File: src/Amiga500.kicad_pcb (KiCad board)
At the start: 2 copper layers, 365.8 x 254 mm, 367 parts, among them CN1 LEFT_JOY, CN10 COMPOSITE, CN11 INTERNAL_FLOPPY, CN12 FLOPPY_POWER, CN13 KEYBOARD, CN14 IDE_POWER, CN15 IDE_I/F, CN2 RIGHT_JOY, CN3 RIGHT, CN4 LEFT, CN5 EXTFLOPPY_DB23F, CN6 SERIAL_DB25M, CN7 PARALLEL_DB25F, CN8 POWER, CN9 VIDEO_DB23M, J90 DRIVE_SWITCHER, J91 Dispatcher_3to1, J92 Dispatcher_3to1, J93 Dispatcher_3to1, J99 CONN_HDACT, P1 EXPANSION BUS, P9 TRAPDOOR, Q301 2N3906, Q321 MPF102, Q331 MPF102, Q501 2N3904, Q502 2N3906, Q503 2N3906, Q711 2N3904, Q921 MMBFJ113, Q931 MMBFJ113, Q99 2N3906, U1 68000D, U10 74LS244, U11 74LS373, U12 74LS244, U13 74LS373, U14 LF347, U15 74LS157, U16 XX4256, U17 XX4256, U18 XX4256, U19 XX4256, U2 FAT_AGNUS_8375, U20 XX4256, U21 XX4256, U22 XX4256, U23 XX4256, U3 PAULA, U32 74LS139, U33 74LS258, U34 74LS373, U35 74LS244, U36 74LS05, U37 74LS32, U38 MC1488, U39 MC1489, U4 DENISE, U40 74LS245, U41 74LS245, U42 NE555, U5 GARY_5719, U6 ROM, U7 VIA_8520, U8 VIA_8520, U9 MSM6242B, U94 74HCT14, X1 XTAL, Y9 32768

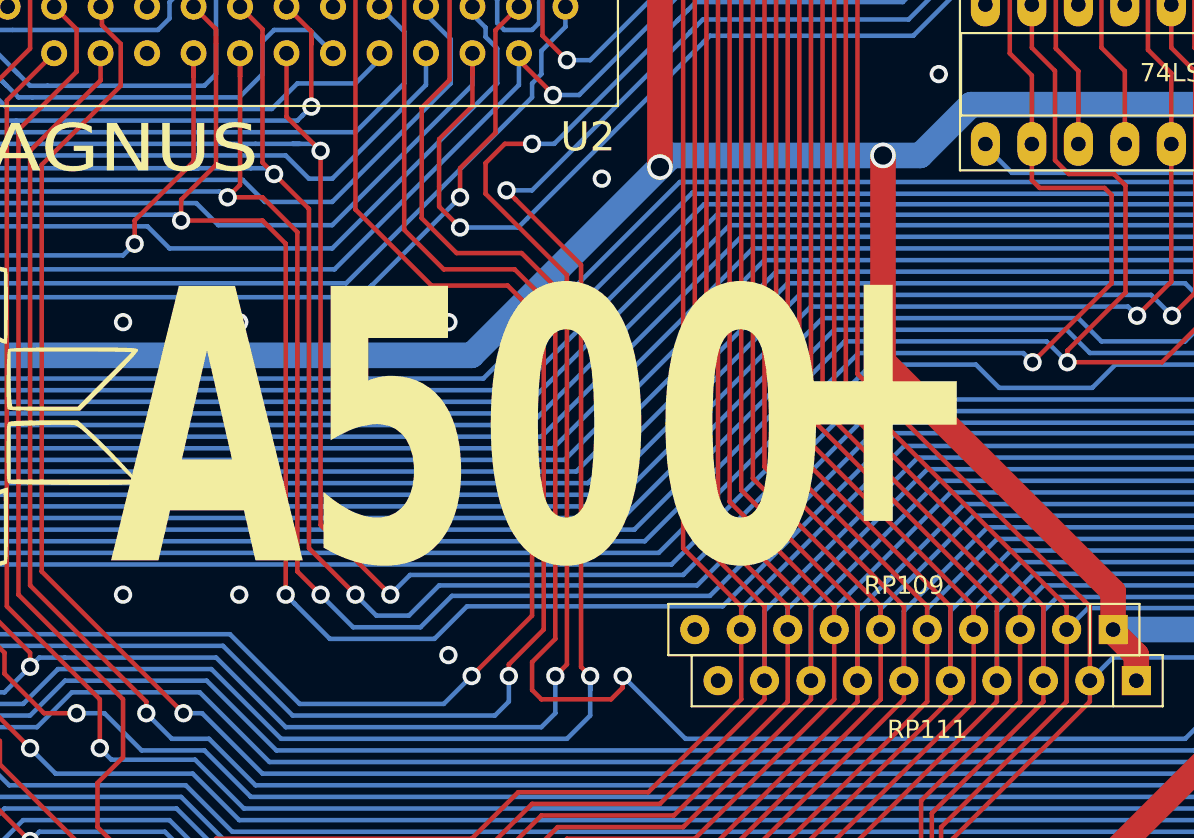
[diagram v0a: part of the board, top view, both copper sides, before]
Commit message: changed silkscreen thickness
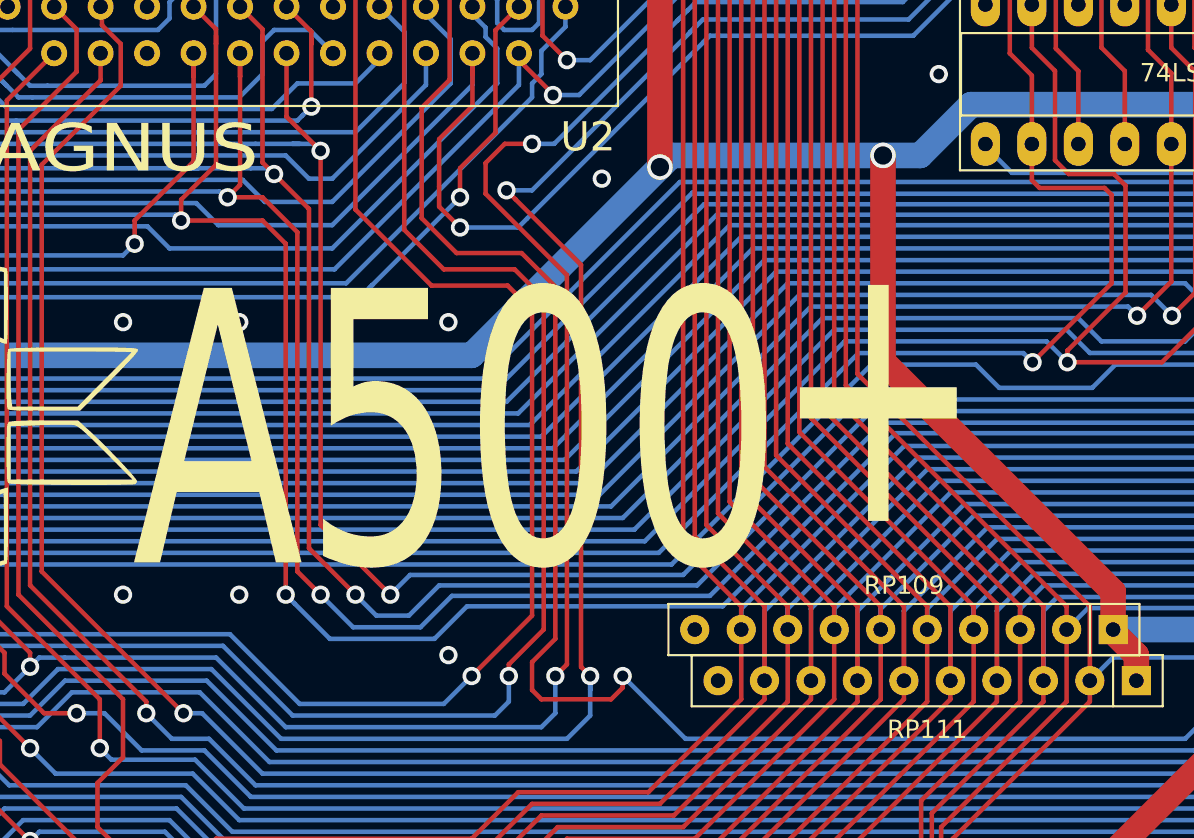
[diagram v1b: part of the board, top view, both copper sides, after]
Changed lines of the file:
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@@
 			(drillshape 0)
 			(scaleselection 1)
-			(outputdirectory "gerbers/")
+			(outputdirectory "../gerbers/")
 		)
 	)
@@
 			(font
 				(size 15 10)
-				(thickness 1.5)
-				(bold yes)
+				(thickness 0.5)
 			)
 			(justify left)
@@
 	)
 	(gr_text "A500"
-		(at 129.1971 212.6742 0)
+		(at 130.4095 212.783 0)
 		(layer "F.SilkS")
 		(effects
 			(font
 				(size 15 10)
-				(thickness 1.5)
-				(bold yes)
+				(thickness 0.5)
 			)
 			(justify left)
